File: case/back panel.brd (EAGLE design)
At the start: 165 x 30.1 mm, 3 parts

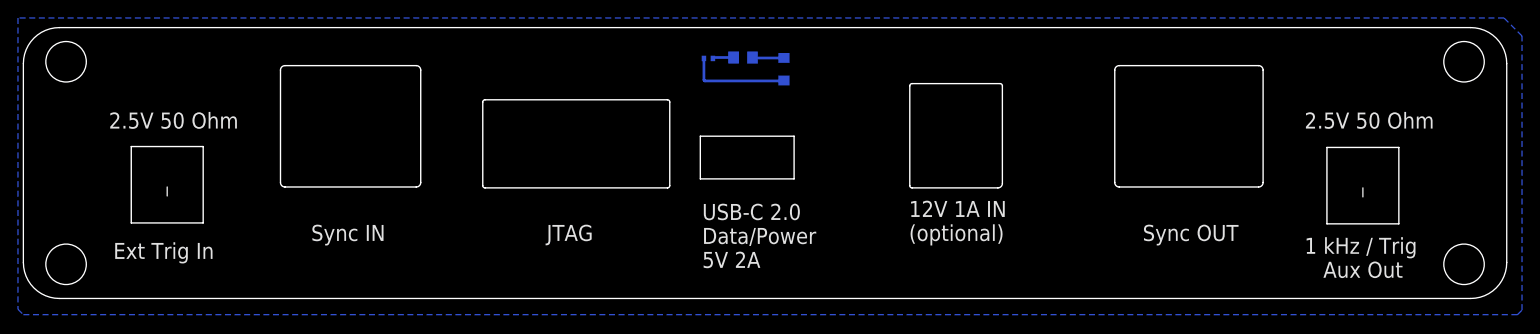
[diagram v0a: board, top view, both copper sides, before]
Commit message: add gnd near screw holes
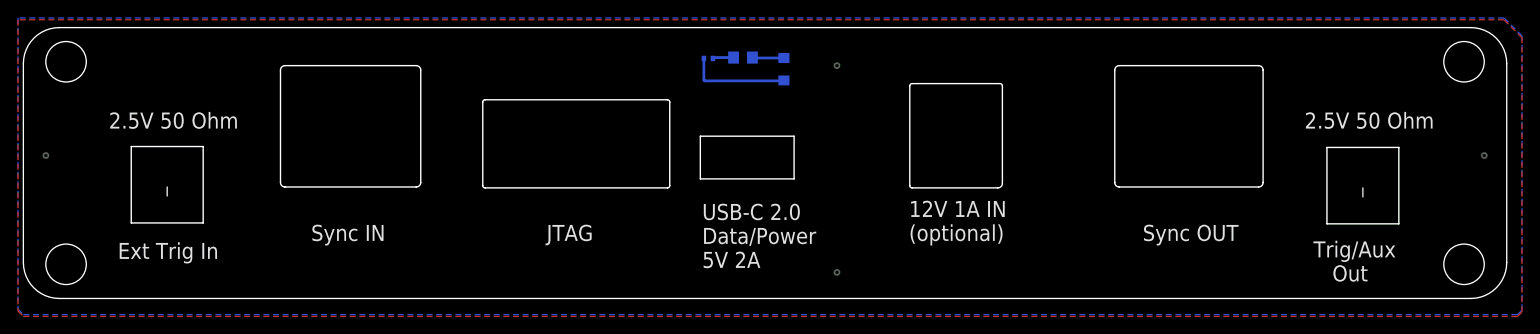
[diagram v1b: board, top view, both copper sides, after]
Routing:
- net GND: vias 0 -> 4
- added copper zone on layer 1, net GND
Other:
- board text added: "Trig/Aux Out"
- board text removed: "1 kHz / Trig Aux Out"

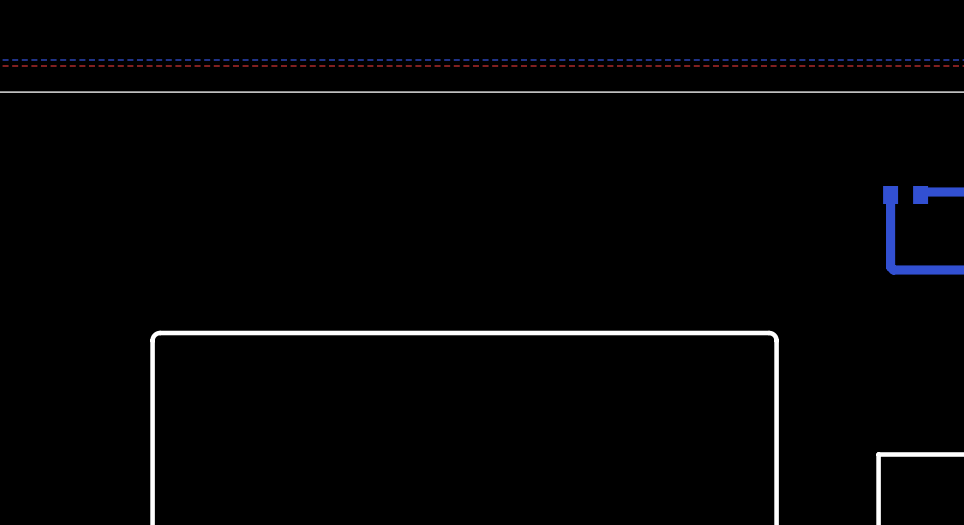
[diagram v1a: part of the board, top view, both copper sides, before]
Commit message: add fcc ce ukca markings
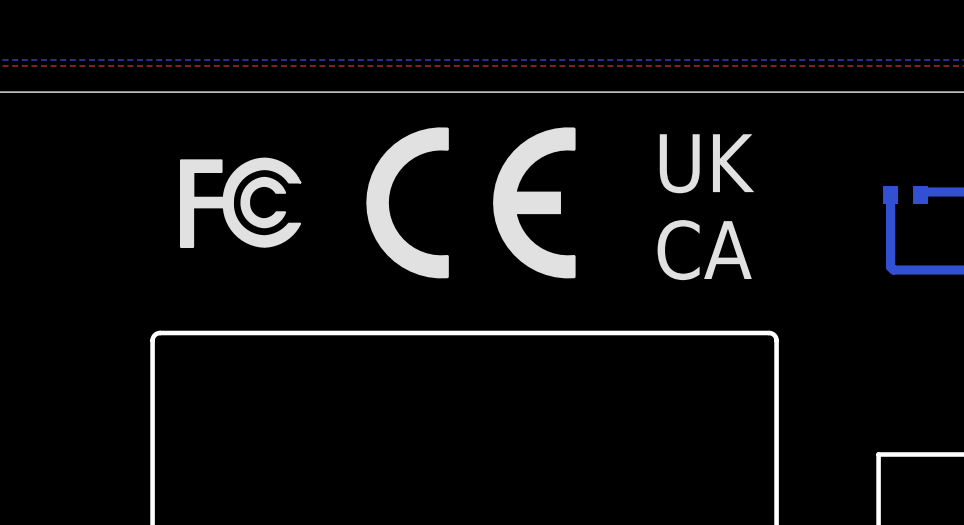
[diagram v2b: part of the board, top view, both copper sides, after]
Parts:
- added U$1: (no value), logo:CE_5MM
- added U$2: (no value), logo:FCC_6.1X16MM
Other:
- board text added: "UK CA"
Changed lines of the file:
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@@
 <drawing>
 <settings>
-<setting alwaysvectorfont="no"/>
+<setting alwaysvectorfont="yes"/>
 <setting verticaltext="up"/>
 </settings>
@@
 <vertex x="164.3" y="-1.4"/>
 </polygon>
+<text x="65.3" y="24" size="1.9304" layer="21" ratio="16">UK
+CA</text>
 </plain>
 <attributes>
@@
 <element name="R1" library="FlashPCB_Resistors" package="RES-0402" value="3.3k" x="73.7" y="26.8" smashed="yes" rot="MR0"/>
 <element name="C2" library="Nordic_nRF" library_urn="urn:adsk.eagle:library:169009" package="RESC0805_N" package3d_urn="urn:adsk.eagle:package:2593736/1" value="10uF" x="77.5" y="26.9" smashed="yes" rot="MR0"/>
+<element name="U$1" library="logo" library_urn="urn:adsk.eagle:library:264" package="CE_5MM" value="" x="55.7" y="24" smashed="yes"/>
+<element name="U$2" library="logo" package="FCC_6.1X16MM" value="" x="48.6" y="24" smashed="yes"/>
 </elements>
 <signals>

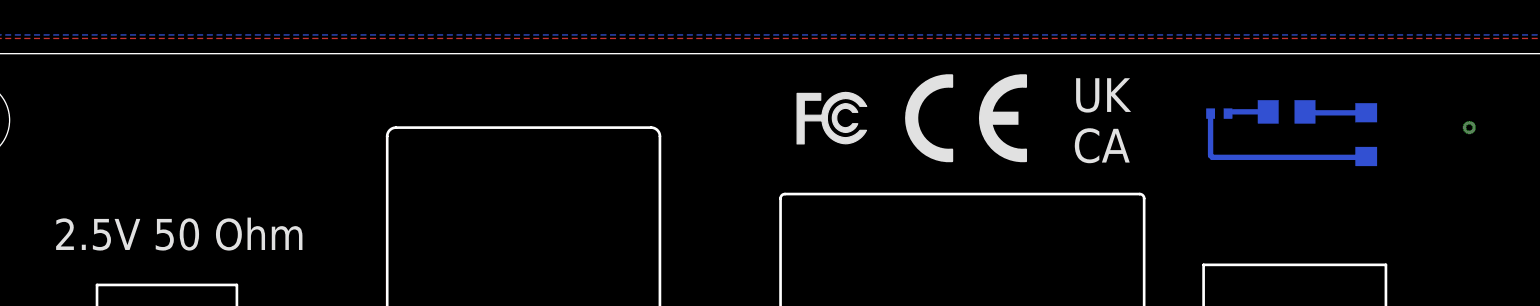
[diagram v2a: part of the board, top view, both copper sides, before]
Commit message: update fcc marking
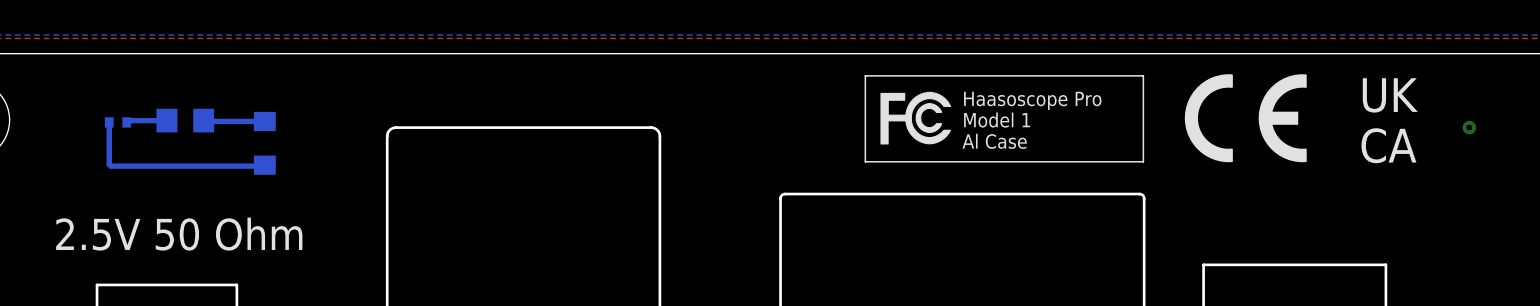
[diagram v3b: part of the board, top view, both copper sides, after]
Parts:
- moved C2 63.0 mm to (14.5, 26.4)
- moved R1 63.0 mm to (10.7, 26.3)
- moved D1 63.0 mm to (19.1, 25.1)
- moved U$1 16.0 mm to (71.7, 24.0)
- moved U$2 4.80 mm to (53.4, 24.0)
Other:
- board text added: "Haasoscope Pro Model 1 Al Case"
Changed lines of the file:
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@@
 <vertex x="164.3" y="-1.4"/>
 </polygon>
-<text x="65.3" y="24" size="1.9304" layer="21" ratio="16">UK
+<text x="81.7" y="24" size="1.9304" layer="21" ratio="16">UK
 CA</text>
+<text x="59" y="24.8" size="0.8128" layer="21">Haasoscope Pro
+Model 1
+Al Case</text>
 </plain>
 <attributes>
@@
 </autorouter>
 <elements>
-<element name="D1" library="MF_LEDs" package="LED0805" value="green" x="82.1" y="25.6" smashed="yes" rot="MR90">
-<attribute name="HOUSEPART" value="NO" x="88.5" y="22.6" size="1.778" layer="28" rot="MR90" display="off"/>
-<attribute name="MPN" value="" x="88.5" y="22.6" size="1.778" layer="28" rot="MR90" display="off"/>
-<attribute name="POPULATE" value="1" x="88.5" y="22.6" size="1.778" layer="28" rot="MR90" display="off"/>
-<attribute name="URL" value="" x="88.5" y="22.6" size="1.778" layer="28" rot="MR90" display="off"/>
+<element name="D1" library="MF_LEDs" package="LED0805" value="green" x="19.1" y="25.1" smashed="yes" rot="MR90">
+<attribute name="HOUSEPART" value="NO" x="25.5" y="22.1" size="1.778" layer="28" rot="MR90" display="off"/>
+<attribute name="MPN" value="" x="25.5" y="22.1" size="1.778" layer="28" rot="MR90" display="off"/>
+<attribute name="POPULATE" value="1" x="25.5" y="22.1" size="1.778" layer="28" rot="MR90" display="off"/>
+<attribute name="URL" value="" x="25.5" y="22.1" size="1.778" layer="28" rot="MR90" display="off"/>
 </element>
-<element name="R1" library="FlashPCB_Resistors" package="RES-0402" value="3.3k" x="73.7" y="26.8" smashed="yes" rot="MR0"/>
-<element name="C2" library="Nordic_nRF" library_urn="urn:adsk.eagle:library:169009" package="RESC0805_N" package3d_urn="urn:adsk.eagle:package:2593736/1" value="10uF" x="77.5" y="26.9" smashed="yes" rot="MR0"/>
-<element name="U$1" library="logo" library_urn="urn:adsk.eagle:library:264" package="CE_5MM" value="" x="55.7" y="24" smashed="yes"/>
-<element name="U$2" library="logo" package="FCC_6.1X16MM" value="" x="48.6" y="24" smashed="yes"/>
+<element name="R1" library="FlashPCB_Resistors" package="RES-0402" value="3.3k" x="10.7" y="26.3" smashed="yes" rot="MR0"/>
+<element name="C2" library="Nordic_nRF" library_urn="urn:adsk.eagle:library:169009" package="RESC0805_N" package3d_urn="urn:adsk.eagle:package:2593736/1" value="10uF" x="14.5" y="26.4" smashed="yes" rot="MR0"/>
+<element name="U$1" library="logo" library_urn="urn:adsk.eagle:library:264" package="CE_5MM" value="" x="71.7" y="24" smashed="yes"/>
+<element name="U$2" library="logo" library_urn="urn:adsk.eagle:library:264" package="FCC_6.1X16MM" value="" x="53.4" y="24" smashed="yes"/>
 </elements>
 <signals>
@@
 <contactref element="R1" pad="P$1"/>
 <contactref element="C2" pad="2"/>
-<wire x1="76.5" y1="26.9" x2="74.3" y2="26.9" width="0.3048" layer="16"/>
-<wire x1="74.3" y1="26.9" x2="74.2" y2="26.8" width="0.3048" layer="16"/>
+<wire x1="13.5" y1="26.4" x2="11.3" y2="26.4" width="0.3048" layer="16"/>
+<wire x1="11.3" y1="26.4" x2="11.2" y2="26.3" width="0.3048" layer="16"/>
 <polygon width="0.1524" layer="16">
 <vertex x="-3.1" y="31.3"/>
@@
 <contactref element="D1" pad="ANODE"/>
 <contactref element="C2" pad="1"/>
-<wire x1="82.1" y1="26.85" x2="78.65" y2="26.85" width="0.3048" layer="16"/>
-<wire x1="78.65" y1="26.85" x2="78.6" y2="26.9" width="0.3048" layer="16"/>
+<wire x1="19.1" y1="26.35" x2="15.65" y2="26.35" width="0.3048" layer="16"/>
+<wire x1="15.65" y1="26.35" x2="15.6" y2="26.4" width="0.3048" layer="16"/>
 </signal>
 <signal name="N$7">
 <contactref element="D1" pad="CATHODE"/>
 <contactref element="R1" pad="P$2"/>
-<wire x1="73.2" y1="26.8" x2="73.2" y2="24.4" width="0.3048" layer="16"/>
-<wire x1="73.2" y1="24.4" x2="73.3" y2="24.3" width="0.3048" layer="16"/>
-<wire x1="73.3" y1="24.3" x2="82.05" y2="24.3" width="0.3048" layer="16"/>
-<wire x1="82.05" y1="24.3" x2="82.1" y2="24.35" width="0.3048" layer="16"/>
+<wire x1="10.2" y1="26.3" x2="10.2" y2="23.9" width="0.3048" layer="16"/>
+<wire x1="10.2" y1="23.9" x2="10.3" y2="23.8" width="0.3048" layer="16"/>
+<wire x1="10.3" y1="23.8" x2="19.05" y2="23.8" width="0.3048" layer="16"/>
+<wire x1="19.05" y1="23.8" x2="19.1" y2="23.85" width="0.3048" layer="16"/>
 </signal>
 </signals>

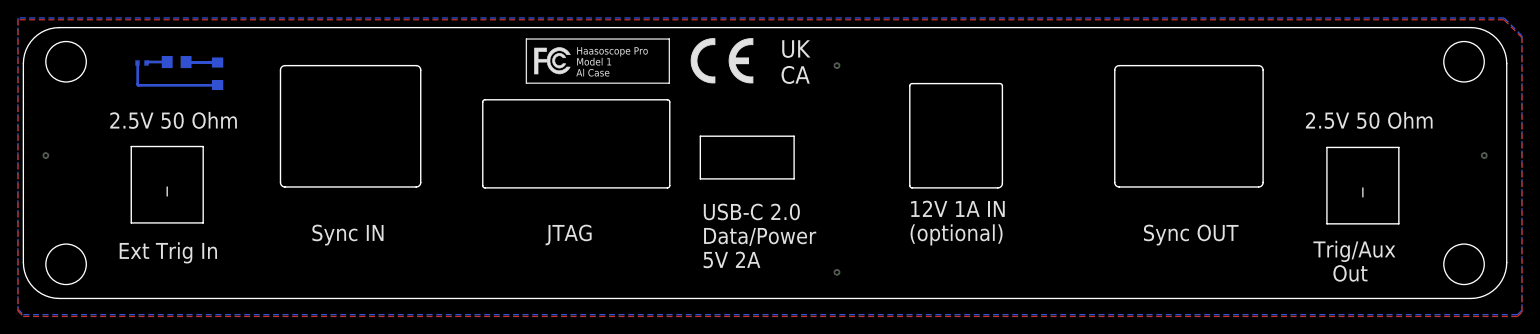
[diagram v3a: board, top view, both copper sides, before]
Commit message: use vias, so gnd is connected to screws (?)
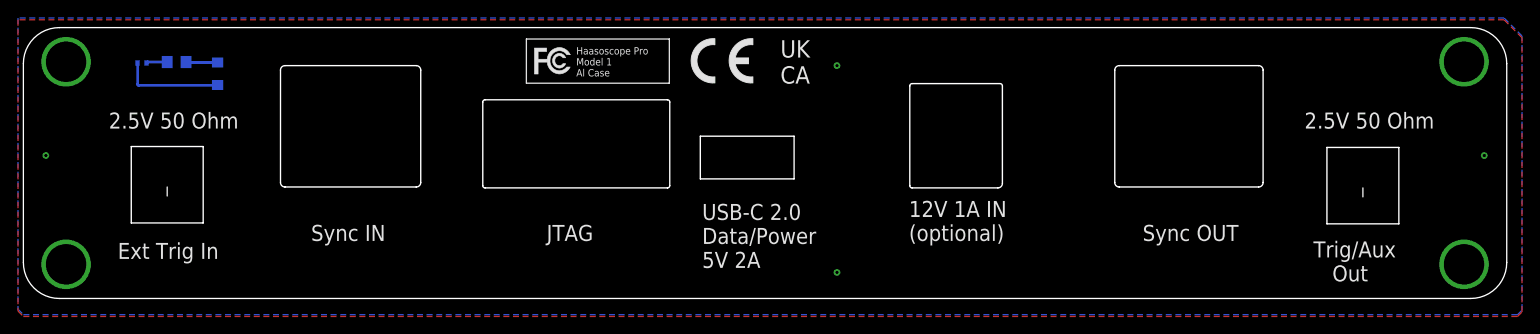
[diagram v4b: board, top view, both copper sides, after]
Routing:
- net GND: vias 4 -> 8
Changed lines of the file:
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@@
 <layer number="27" name="tValues" color="7" fill="1" visible="yes" active="yes"/>
 <layer number="28" name="bValues" color="7" fill="1" visible="yes" active="yes"/>
-<layer number="29" name="tStop" color="7" fill="3" visible="yes" active="yes"/>
+<layer number="29" name="tStop" color="7" fill="3" visible="no" active="yes"/>
 <layer number="30" name="bStop" color="7" fill="6" visible="yes" active="yes"/>
-<layer number="31" name="tCream" color="7" fill="4" visible="yes" active="yes"/>
+<layer number="31" name="tCream" color="7" fill="4" visible="no" active="yes"/>
 <layer number="32" name="bCream" color="7" fill="5" visible="yes" active="yes"/>
 <layer number="33" name="tFinish" color="6" fill="3" visible="yes" active="yes"/>
@@
 <wire x1="158.5" y1="30.23" x2="1.5" y2="30.23" width="0" layer="20"/>
 <wire x1="1.5" y1="30.23" x2="-2.5" y2="26.23" width="0" layer="20" curve="90"/>
-<hole x="2.25" y="26.43" drill="4.5"/>
-<hole x="157.75" y="26.43" drill="4.5"/>
-<hole x="157.75" y="3.9" drill="4.5"/>
-<hole x="2.25" y="3.9" drill="4.5"/>
 <wire x1="72.8" y1="18.15" x2="83.23" y2="18.15" width="0.1524" layer="20"/>
 <wire x1="83.23" y1="18.15" x2="83.23" y2="13.4" width="0.1524" layer="20"/>
@@
 <via x="88" y="26" extent="1-16" drill="0.35"/>
 <via x="88" y="3" extent="1-16" drill="0.35"/>
+<via x="157.75" y="26.43" extent="1-16" drill="4.5"/>
+<via x="157.75" y="3.9" extent="1-16" drill="4.5"/>
+<via x="2.25" y="3.9" extent="1-16" drill="4.5"/>
+<via x="2.25" y="26.43" extent="1-16" drill="4.5"/>
 </signal>
 <signal name="5V">
